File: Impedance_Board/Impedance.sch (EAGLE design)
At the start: 40 parts, among them IC1 AD8608ARZ, IC2 INA826AID, U4 MC74VHC1GT66DTT1

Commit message: Board Updates
All LEDs at same location
Separated analog and digital ground
Updated impedance components
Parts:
- C1, C13, C5, C9: device rcl:C-EUC0603 -> SparkFun-Capacitors:10UF-0603-6.3V-20%
- C12, C2, C4, C8: device rcl:C-EUC0603 -> SparkFun-Capacitors:0.1UF-0603-25V-5%
- C3: value 0.1uF -> 10nF; device SparkFun-Capacitors:0.1UF-0603-25V-(+80/-20%) -> SparkFun-Capacitors:10NF-0603-50V-10%
- R10, R9: value 47k -> 10k; device SparkFun-Resistors:47KOHM-0603-1/10W-1% -> SparkFun-Resistors:10KOHM-0603-1/10W-1%
- R11: value 1k -> 270k; device SparkFun-Resistors:1KOHM-0603-1/10W-1% -> SparkFun-Resistors:220KOHM-0603-1/10W-1%
- R5, R6: value 47k -> 100k; device SparkFun-Resistors:47KOHM-0603-1/10W-1% -> SparkFun-Resistors:100KOHM-0603-1/10W-1%
- R7: value 3.9k -> 200k; device SparkFun-Resistors:3.9KOHM-0603-1/10W-1% -> SparkFun-Resistors:200KOHM-0603-1/10W-1%
- R8: value 5.6k -> 1k; device SparkFun-Resistors:5.6KOHM-0603-1/10W-1% -> SparkFun-Resistors:1KOHM-0603-1/10W-1%
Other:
- moved on the sheet: C1, C12, C13, C2, C4, C5, C8, C9

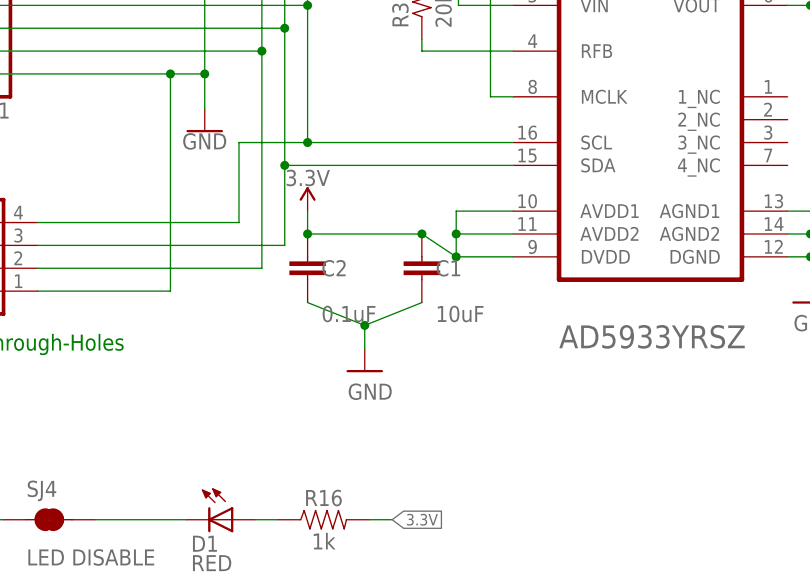
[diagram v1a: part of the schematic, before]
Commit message: Board Updates
Separated analog and digital ground
Updated routing
Updated silk labeling
Sound board with ES8388 included
Impedance and ECG board
Working on IMU board
Working on Environmental Airquality board
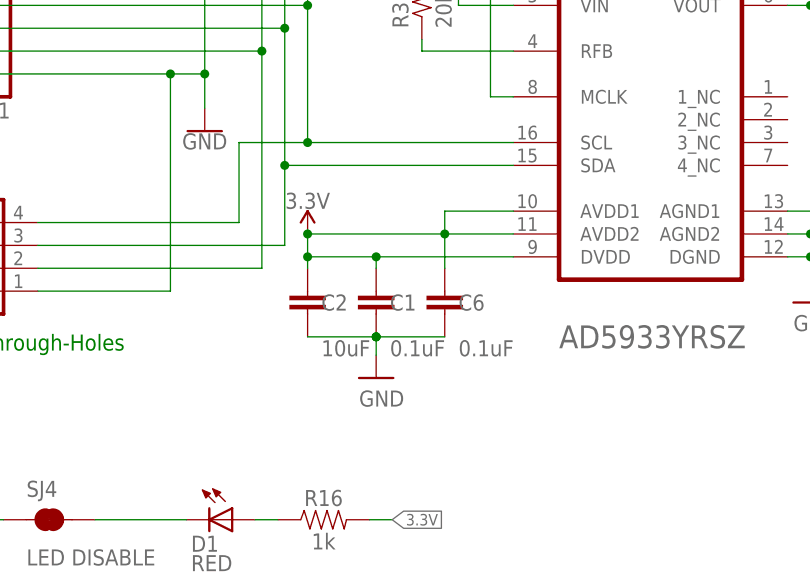
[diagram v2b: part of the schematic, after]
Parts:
- added C6: 0.1uF, SparkFun-Capacitors:0.1UF-0603-25V-(+80/-20%)
- C1: value 10uF -> 0.1uF; device SparkFun-Capacitors:10UF-0603-6.3V-20% -> SparkFun-Capacitors:0.1UF-0603-25V-(+80/-20%)
- C2: value 0.1uF -> 10uF; device SparkFun-Capacitors:0.1UF-0603-25V-5% -> SparkFun-Capacitors:10UF-0603-6.3V-20%
- SJ4: device SparkFun-Jumpers:JUMPER-SMT_2_NC_TRACE_NO-SILK -> SparkFun-Jumpers:JUMPER-SMT_2_NC_TRACE_SILK
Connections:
- net 3.3V: now also C6.1
- net GND: now also C6.2
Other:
- moved on the sheet: C1, C2
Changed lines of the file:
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@@
 <part name="R1" library="SparkFun-Resistors" library_urn="urn:adsk.eagle:library:532" deviceset="4.7KOHM" device="-0603-1/10W-1%" package3d_urn="urn:adsk.eagle:package:39650/1" value="4.7k"/>
 <part name="R2" library="SparkFun-Resistors" library_urn="urn:adsk.eagle:library:532" deviceset="4.7KOHM" device="-0603-1/10W-1%" package3d_urn="urn:adsk.eagle:package:39650/1" value="4.7k"/>
-<part name="C1" library="SparkFun-Capacitors" library_urn="urn:adsk.eagle:library:510" deviceset="10UF" device="-0603-6.3V-20%" package3d_urn="urn:adsk.eagle:package:37414/1" value="10uF"/>
-<part name="C2" library="SparkFun-Capacitors" library_urn="urn:adsk.eagle:library:510" deviceset="0.1UF" device="-0603-25V-5%" package3d_urn="urn:adsk.eagle:package:37414/1" value="0.1uF"/>
+<part name="C1" library="SparkFun-Capacitors" library_urn="urn:adsk.eagle:library:510" deviceset="0.1UF" device="-0603-25V-(+80/-20%)" package3d_urn="urn:adsk.eagle:package:37414/1" value="0.1uF"/>
+<part name="C2" library="SparkFun-Capacitors" library_urn="urn:adsk.eagle:library:510" deviceset="10UF" device="-0603-6.3V-20%" package3d_urn="urn:adsk.eagle:package:37414/1" value="10uF"/>
 <part name="R3" library="SparkFun-Resistors" library_urn="urn:adsk.eagle:library:532" deviceset="20KOHM" device="-0603-1/10W-1%" package3d_urn="urn:adsk.eagle:package:39650/1" value="20k"/>
 <part name="R4" library="SparkFun-Resistors" library_urn="urn:adsk.eagle:library:532" deviceset="20KOHM" device="-0603-1/10W-1%" package3d_urn="urn:adsk.eagle:package:39650/1" value="20k"/>
@@
 <part name="D1" library="SparkFun-LED" deviceset="LED-RED" device="0603" value="RED"/>
 <part name="GND4" library="SparkFun-Aesthetics" deviceset="GND" device=""/>
-<part name="SJ4" library="SparkFun-Jumpers" library_urn="urn:adsk.eagle:library:528" deviceset="JUMPER-SMT_2_NC_TRACE" device="_NO-SILK" package3d_urn="urn:adsk.eagle:package:39286/1" value="LED DISABLE"/>
+<part name="SJ4" library="SparkFun-Jumpers" library_urn="urn:adsk.eagle:library:528" deviceset="JUMPER-SMT_2_NC_TRACE" device="_SILK" package3d_urn="urn:adsk.eagle:package:39281/1" value="LED DISABLE"/>
 <part name="JP1" library="SparkFun-Jumpers" library_urn="urn:adsk.eagle:library:528" deviceset="JUMPER-SMT_3_1-NC_TRACE" device="_NO-SILK" package3d_urn="urn:adsk.eagle:package:39287/1"/>
 <part name="IC1" library="AD8608ARZ" deviceset="AD8608ARZ" device=""/>
@@
 <part name="FRAME1" library="SparkFun-Aesthetics" library_urn="urn:adsk.eagle:library:507" deviceset="FRAME-LETTER" device="NO_PACKAGE" package3d_urn="urn:adsk.eagle:package:37104/1"/>
 <part name="JP2" library="SparkFun-Jumpers" library_urn="urn:adsk.eagle:library:528" deviceset="JUMPER-SMT_3_1-NC_TRACE" device="_NO-SILK" package3d_urn="urn:adsk.eagle:package:39287/1"/>
+<part name="C6" library="SparkFun-Capacitors" library_urn="urn:adsk.eagle:library:510" deviceset="0.1UF" device="-0603-25V-(+80/-20%)" package3d_urn="urn:adsk.eagle:package:37414/1" value="0.1uF"/>
 </parts>
 <sheets>
@@
 <attribute name="VALUE" x="-81.534" y="36.576" size="1.778" layer="96" rot="R90"/>
 </instance>
-<instance part="C1" gate="G$1" x="-53.34" y="-21.59" smashed="yes">
-<attribute name="NAME" x="-51.816" y="-21.209" size="1.778" layer="95"/>
-<attribute name="VALUE" x="-51.816" y="-26.289" size="1.778" layer="96"/>
-</instance>
-<instance part="C2" gate="G$1" x="-66.04" y="-21.59" smashed="yes">
-<attribute name="NAME" x="-64.516" y="-21.209" size="1.778" layer="95"/>
-<attribute name="VALUE" x="-64.516" y="-26.289" size="1.778" layer="96"/>
+<instance part="C1" gate="G$1" x="-58.42" y="-25.4" smashed="yes">
+<attribute name="NAME" x="-56.896" y="-25.019" size="1.778" layer="95"/>
+<attribute name="VALUE" x="-56.896" y="-30.099" size="1.778" layer="96"/>
+</instance>
+<instance part="C2" gate="G$1" x="-66.04" y="-25.4" smashed="yes">
+<attribute name="NAME" x="-64.516" y="-25.019" size="1.778" layer="95"/>
+<attribute name="VALUE" x="-64.516" y="-30.099" size="1.778" layer="96"/>
 </instance>
 <instance part="R3" gate="G$1" x="-53.34" y="10.16" smashed="yes" rot="R90">
@@
 <attribute name="VALUE" x="12.065" y="-9.525" size="1.778" layer="96"/>
 </instance>
-<instance part="SUPPLY2" gate="1" x="-59.69" y="-31.75" smashed="yes">
-<attribute name="VALUE" x="-61.595" y="-34.925" size="1.778" layer="96"/>
-</instance>
-<instance part="SUPPLY3" gate="G$1" x="-66.04" y="-13.97" smashed="yes">
-<attribute name="VALUE" x="-66.04" y="-11.176" size="1.778" layer="96" align="bottom-center"/>
+<instance part="SUPPLY2" gate="1" x="-58.42" y="-32.512" smashed="yes">
+<attribute name="VALUE" x="-60.325" y="-35.687" size="1.778" layer="96"/>
+</instance>
+<instance part="SUPPLY3" gate="G$1" x="-66.04" y="-16.51" smashed="yes">
+<attribute name="VALUE" x="-66.04" y="-13.716" size="1.778" layer="96" align="bottom-center"/>
 </instance>
 <instance part="SUPPLY5" gate="1" x="-10.16" y="-24.13" smashed="yes">
@@
 <attribute name="NAME" x="-1.651" y="-10.16" size="1.778" layer="95" font="vector" rot="MR180"/>
 <attribute name="VALUE" x="-0.889" y="-10.16" size="1.778" layer="96" font="vector" rot="MR270" align="top-left" display="off"/>
+</instance>
+<instance part="C6" gate="G$1" x="-50.8" y="-25.4" smashed="yes">
+<attribute name="NAME" x="-49.276" y="-25.019" size="1.778" layer="95"/>
+<attribute name="VALUE" x="-49.276" y="-30.099" size="1.778" layer="96"/>
 </instance>
 </instances>
@@
 <pinref part="C2" gate="G$1" pin="2"/>
 <pinref part="C1" gate="G$1" pin="2"/>
-<wire x1="-66.04" y1="-24.13" x2="-59.69" y2="-26.67" width="0.1524" layer="91"/>
-<wire x1="-59.69" y1="-26.67" x2="-53.34" y2="-24.13" width="0.1524" layer="91"/>
-<wire x1="-59.69" y1="-26.67" x2="-59.69" y2="-29.21" width="0.1524" layer="91"/>
-<junction x="-59.69" y="-26.67"/>
+<wire x1="-66.04" y1="-27.94" x2="-58.42" y2="-27.94" width="0.1524" layer="91"/>
+<wire x1="-58.42" y1="-27.94" x2="-58.42" y2="-29.972" width="0.1524" layer="91"/>
+<junction x="-58.42" y="-27.94"/>
 <pinref part="SUPPLY2" gate="1" pin="GND"/>
+<pinref part="C6" gate="G$1" pin="2"/>
+<wire x1="-58.42" y1="-27.94" x2="-50.8" y2="-27.94" width="0.1524" layer="91"/>
+<junction x="-58.42" y="-27.94"/>
 </segment>
 <segment>
@@
 </segment>
 <segment>
+<pinref part="SUPPLY3" gate="G$1" pin="3.3V"/>
+<pinref part="C2" gate="G$1" pin="1"/>
+<wire x1="-66.04" y1="-20.32" x2="-66.04" y2="-19.05" width="0.1524" layer="91"/>
+<pinref part="AD5933" gate="G$0" pin="AVDD2"/>
+<wire x1="-66.04" y1="-19.05" x2="-66.04" y2="-16.51" width="0.1524" layer="91"/>
+<wire x1="-43.18" y1="-16.51" x2="-50.8" y2="-16.51" width="0.1524" layer="91"/>
+<pinref part="AD5933" gate="G$0" pin="AVDD1"/>
+<wire x1="-50.8" y1="-13.97" x2="-50.8" y2="-16.51" width="0.1524" layer="91"/>
+<wire x1="-43.18" y1="-13.97" x2="-50.8" y2="-13.97" width="0.1524" layer="91"/>
+<pinref part="C6" gate="G$1" pin="1"/>
+<wire x1="-50.8" y1="-20.32" x2="-50.8" y2="-16.51" width="0.1524" layer="91"/>
+<junction x="-50.8" y="-16.51"/>
+<wire x1="-66.04" y1="-16.51" x2="-50.8" y2="-16.51" width="0.1524" layer="91"/>
+<junction x="-66.04" y="-16.51"/>
+<pinref part="AD5933" gate="G$0" pin="DVDD"/>
 <pinref part="C1" gate="G$1" pin="1"/>
-<pinref part="AD5933" gate="G$0" pin="DVDD"/>
-<wire x1="-53.34" y1="-16.51" x2="-49.53" y2="-19.05" width="0.1524" layer="91"/>
-<pinref part="AD5933" gate="G$0" pin="AVDD2"/>
-<wire x1="-49.53" y1="-19.05" x2="-43.18" y2="-19.05" width="0.1524" layer="91"/>
-<wire x1="-43.18" y1="-16.51" x2="-49.53" y2="-16.51" width="0.1524" layer="91"/>
-<wire x1="-49.53" y1="-16.51" x2="-49.53" y2="-19.05" width="0.1524" layer="91"/>
-<junction x="-49.53" y="-19.05"/>
-<pinref part="AD5933" gate="G$0" pin="AVDD1"/>
-<wire x1="-43.18" y1="-13.97" x2="-49.53" y2="-13.97" width="0.1524" layer="91"/>
-<wire x1="-49.53" y1="-13.97" x2="-49.53" y2="-16.51" width="0.1524" layer="91"/>
-<junction x="-49.53" y="-16.51"/>
-<pinref part="C2" gate="G$1" pin="1"/>
-<wire x1="-66.04" y1="-16.51" x2="-53.34" y2="-16.51" width="0.1524" layer="91"/>
-<junction x="-53.34" y="-16.51"/>
-<wire x1="-66.04" y1="-16.51" x2="-66.04" y2="-13.97" width="0.1524" layer="91"/>
-<junction x="-66.04" y="-16.51"/>
-<pinref part="SUPPLY3" gate="G$1" pin="3.3V"/>
-</segment>
-<segment>
+<wire x1="-43.18" y1="-19.05" x2="-58.42" y2="-19.05" width="0.1524" layer="91"/>
+<wire x1="-58.42" y1="-19.05" x2="-58.42" y2="-20.32" width="0.1524" layer="91"/>
+<wire x1="-58.42" y1="-19.05" x2="-66.04" y2="-19.05" width="0.1524" layer="91"/>
+<junction x="-58.42" y="-19.05"/>
+<junction x="-66.04" y="-19.05"/>
+</segment>
+<segment>

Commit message: Production Updates
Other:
- note added: "AMP_FB"
- note added: "Amp_Buffer"
- note added: "Amp_REFGEN"
- note added: "Amp_VCC"
- moved on the sheet: C12, C13, C4, C5, C8, C9
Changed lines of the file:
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@@
 <drawing>
 <settings>
-<setting alwaysvectorfont="no"/>
+<setting alwaysvectorfont="yes"/>
 <setting verticaltext="up"/>
 </settings>
@@
 <text x="24.638" y="32.258" size="1.778" layer="91">Switch
 Direct vs Transimpedance</text>
+<text x="55.88" y="40.64" size="1.778" layer="91">Amp_VCC</text>
+<text x="55.88" y="45.72" size="1.778" layer="91">Amp_REFGEN</text>
+<text x="38.1" y="45.72" size="1.778" layer="91">Amp_Buffer</text>
+<text x="38.1" y="40.64" size="1.778" layer="91">AMP_FB</text>
 </plain>
 <instances>
@@
 <attribute name="VALUE" x="20.574" y="-11.176" size="1.778" layer="96" rot="MR0" align="bottom-center"/>
 </instance>
-<instance part="C4" gate="G$1" x="20.574" y="-19.05" smashed="yes" rot="MR0">
-<attribute name="NAME" x="19.05" y="-18.669" size="1.778" layer="95" rot="MR0"/>
-<attribute name="VALUE" x="19.05" y="-23.749" size="1.778" layer="96" rot="MR0"/>
-</instance>
-<instance part="C5" gate="G$1" x="9.144" y="-19.05" smashed="yes" rot="MR0">
-<attribute name="NAME" x="7.62" y="-18.669" size="1.778" layer="95" rot="MR0"/>
-<attribute name="VALUE" x="7.62" y="-23.749" size="1.778" layer="96" rot="MR0"/>
+<instance part="C4" gate="G$1" x="20.574" y="-21.59" smashed="yes" rot="MR0">
+<attribute name="NAME" x="19.05" y="-21.209" size="1.778" layer="95" rot="MR0"/>
+<attribute name="VALUE" x="19.05" y="-26.289" size="1.778" layer="96" rot="MR0"/>
+</instance>
+<instance part="C5" gate="G$1" x="9.144" y="-21.59" smashed="yes" rot="MR0">
+<attribute name="NAME" x="7.62" y="-21.209" size="1.778" layer="95" rot="MR0"/>
+<attribute name="VALUE" x="7.62" y="-26.289" size="1.778" layer="96" rot="MR0"/>
 </instance>
 <instance part="SUPPLY8" gate="1" x="14.224" y="-29.21" smashed="yes" rot="MR0">
@@
 <attribute name="VALUE" x="88.265" y="-44.831" size="1.778" layer="96"/>
 </instance>
-<instance part="C8" gate="G$1" x="16.51" y="46.99" smashed="yes" rot="MR0">
-<attribute name="NAME" x="14.986" y="47.371" size="1.778" layer="95" rot="MR0"/>
-<attribute name="VALUE" x="14.986" y="42.291" size="1.778" layer="96" rot="MR0"/>
-</instance>
-<instance part="C9" gate="G$1" x="8.89" y="46.99" smashed="yes" rot="MR0">
-<attribute name="NAME" x="7.366" y="47.371" size="1.778" layer="95" rot="MR0"/>
-<attribute name="VALUE" x="7.366" y="42.291" size="1.778" layer="96" rot="MR0"/>
+<instance part="C8" gate="G$1" x="16.51" y="44.45" smashed="yes" rot="MR0">
+<attribute name="NAME" x="14.986" y="44.831" size="1.778" layer="95" rot="MR0"/>
+<attribute name="VALUE" x="14.986" y="39.751" size="1.778" layer="96" rot="MR0"/>
+</instance>
+<instance part="C9" gate="G$1" x="8.89" y="44.45" smashed="yes" rot="MR0">
+<attribute name="NAME" x="7.366" y="44.831" size="1.778" layer="95" rot="MR0"/>
+<attribute name="VALUE" x="7.366" y="39.751" size="1.778" layer="96" rot="MR0"/>
 </instance>
 <instance part="SUPPLY14" gate="G$1" x="16.51" y="50.8" smashed="yes" rot="MR0">
@@
 <attribute name="VALUE" x="-55.88" y="20.32" size="1.778" layer="96" font="vector" rot="MR0" display="off"/>
 </instance>
-<instance part="C12" gate="G$1" x="-55.88" y="41.91" smashed="yes" rot="MR0">
-<attribute name="NAME" x="-57.404" y="42.291" size="1.778" layer="95" rot="MR0"/>
-<attribute name="VALUE" x="-57.404" y="37.211" size="1.778" layer="96" rot="MR0"/>
-</instance>
-<instance part="C13" gate="G$1" x="-63.5" y="41.91" smashed="yes" rot="MR0">
-<attribute name="NAME" x="-65.024" y="42.291" size="1.778" layer="95" rot="MR0"/>
-<attribute name="VALUE" x="-65.024" y="37.211" size="1.778" layer="96" rot="MR0"/>
+<instance part="C12" gate="G$1" x="-55.88" y="39.37" smashed="yes" rot="MR0">
+<attribute name="NAME" x="-57.404" y="39.751" size="1.778" layer="95" rot="MR0"/>
+<attribute name="VALUE" x="-57.404" y="34.671" size="1.778" layer="96" rot="MR0"/>
+</instance>
+<instance part="C13" gate="G$1" x="-63.5" y="39.37" smashed="yes" rot="MR0">
+<attribute name="NAME" x="-65.024" y="39.751" size="1.778" layer="95" rot="MR0"/>
+<attribute name="VALUE" x="-65.024" y="34.671" size="1.778" layer="96" rot="MR0"/>
 </instance>
 <instance part="SUPPLY26" gate="1" x="-59.69" y="31.75" smashed="yes" rot="MR0">
@@
 <pinref part="C4" gate="G$1" pin="2"/>
 <pinref part="C5" gate="G$1" pin="2"/>
-<wire x1="20.574" y1="-21.59" x2="14.224" y2="-24.13" width="0.1524" layer="91"/>
-<wire x1="14.224" y1="-24.13" x2="9.144" y2="-21.59" width="0.1524" layer="91"/>
+<wire x1="20.574" y1="-24.13" x2="14.224" y2="-24.13" width="0.1524" layer="91"/>
+<wire x1="14.224" y1="-24.13" x2="9.144" y2="-24.13" width="0.1524" layer="91"/>
 <wire x1="14.224" y1="-24.13" x2="14.224" y2="-26.67" width="0.1524" layer="91"/>
 <junction x="14.224" y="-24.13"/>
@@
 <pinref part="SUPPLY15" gate="1" pin="GND"/>
 <pinref part="C8" gate="G$1" pin="2"/>
-<wire x1="16.51" y1="44.45" x2="12.7" y2="41.91" width="0.1524" layer="91"/>
+<wire x1="16.51" y1="41.91" x2="12.7" y2="41.91" width="0.1524" layer="91"/>
 <wire x1="12.7" y1="41.91" x2="12.7" y2="39.37" width="0.1524" layer="91"/>
 <junction x="12.7" y="41.91"/>
-<wire x1="12.7" y1="41.91" x2="8.89" y2="44.45" width="0.1524" layer="91"/>
+<wire x1="12.7" y1="41.91" x2="8.89" y2="41.91" width="0.1524" layer="91"/>
 </segment>
 <segment>
@@
 <pinref part="C12" gate="G$1" pin="2"/>
 <pinref part="C13" gate="G$1" pin="2"/>
-<wire x1="-55.88" y1="39.37" x2="-59.69" y2="36.83" width="0.1524" layer="91"/>
-<wire x1="-59.69" y1="36.83" x2="-63.5" y2="39.37" width="0.1524" layer="91"/>
+<wire x1="-55.88" y1="36.83" x2="-59.69" y2="36.83" width="0.1524" layer="91"/>
+<wire x1="-59.69" y1="36.83" x2="-63.5" y2="36.83" width="0.1524" layer="91"/>
 <wire x1="-59.69" y1="36.83" x2="-59.69" y2="34.29" width="0.1524" layer="91"/>
 <junction x="-59.69" y="36.83"/>
@@
 <pinref part="SUPPLY7" gate="G$1" pin="3.3V"/>
 <pinref part="C4" gate="G$1" pin="1"/>
-<wire x1="20.574" y1="-13.97" x2="9.144" y2="-13.97" width="0.1524" layer="91"/>
-<junction x="20.574" y="-13.97"/>
+<wire x1="20.574" y1="-16.51" x2="9.144" y2="-16.51" width="0.1524" layer="91"/>
+<junction x="20.574" y="-16.51"/>
 <pinref part="C5" gate="G$1" pin="1"/>
 <pinref part="IC2" gate="G$1" pin="+VS"/>
 <wire x1="63.5" y1="-20.32" x2="64.77" y2="-20.32" width="0.1524" layer="91"/>
 <wire x1="64.77" y1="-20.32" x2="64.77" y2="-16.51" width="0.1524" layer="91"/>
-<wire x1="64.77" y1="-16.51" x2="20.574" y2="-13.97" width="0.1524" layer="91"/>
-<wire x1="20.32" y1="-16.51" x2="20.574" y2="-13.97" width="0.1524" layer="91"/>
+<wire x1="64.77" y1="-16.51" x2="20.574" y2="-16.51" width="0.1524" layer="91"/>
+<wire x1="20.32" y1="-16.51" x2="20.574" y2="-16.51" width="0.1524" layer="91"/>
+<wire x1="20.574" y1="-16.51" x2="20.574" y2="-13.97" width="0.1524" layer="91"/>
 </segment>
 <segment>
@@
 </segment>
 <segment>
-<wire x1="16.51" y1="52.07" x2="16.51" y2="50.8" width="0.1524" layer="91"/>
+<wire x1="16.51" y1="49.53" x2="16.51" y2="50.8" width="0.1524" layer="91"/>
 <pinref part="C8" gate="G$1" pin="1"/>
-<wire x1="16.51" y1="52.07" x2="8.89" y2="52.07" width="0.1524" layer="91"/>
-<junction x="16.51" y="52.07"/>
+<wire x1="16.51" y1="49.53" x2="8.89" y2="49.53" width="0.1524" layer="91"/>
+<junction x="16.51" y="49.53"/>
 <pinref part="C9" gate="G$1" pin="1"/>
 <pinref part="SUPPLY14" gate="G$1" pin="3.3V"/>
@@
 <wire x1="20.574" y1="49.53" x2="20.574" y2="6.35" width="0.1524" layer="91"/>
 <wire x1="20.574" y1="6.35" x2="35.814" y2="6.35" width="0.1524" layer="91"/>
-<wire x1="16.51" y1="52.07" x2="20.574" y2="49.53" width="0.1524" layer="91"/>
+<wire x1="16.51" y1="49.53" x2="20.574" y2="49.53" width="0.1524" layer="91"/>
 </segment>
 <segment>
@@
 <pinref part="C13" gate="G$1" pin="1"/>
 <pinref part="C12" gate="G$1" pin="1"/>
-<wire x1="-55.88" y1="46.99" x2="-63.5" y2="46.99" width="0.1524" layer="91"/>
-<junction x="-55.88" y="46.99"/>
+<wire x1="-55.88" y1="44.45" x2="-63.5" y2="44.45" width="0.1524" layer="91"/>
+<junction x="-55.88" y="44.45"/>
 <pinref part="U4" gate="A" pin="5"/>
 <wire x1="-10.16" y1="40.64" x2="-7.62" y2="40.64" width="0.1524" layer="91"/>
 <wire x1="-7.62" y1="40.64" x2="-7.62" y2="49.53" width="0.1524" layer="91"/>
 <wire x1="-7.62" y1="49.53" x2="-55.88" y2="49.53" width="0.1524" layer="91"/>
-<wire x1="-55.88" y1="49.53" x2="-55.88" y2="46.99" width="0.1524" layer="91"/>
+<wire x1="-55.88" y1="49.53" x2="-55.88" y2="44.45" width="0.1524" layer="91"/>
 <pinref part="SUPPLY23" gate="G$1" pin="3.3V"/>
-<wire x1="-63.5" y1="46.99" x2="-63.5" y2="45.212" width="0.1524" layer="91"/>
-<junction x="-63.5" y="46.99"/>
+<wire x1="-63.5" y1="44.45" x2="-63.5" y2="45.212" width="0.1524" layer="91"/>
+<junction x="-63.5" y="44.45"/>
 </segment>
 </net>
@@
 </segment>
 </net>
+<net name="N$7" class="0">
+<segment>
+<wire x1="35.56" y1="48.26" x2="35.56" y2="43.18" width="0.1524" layer="91"/>
+<wire x1="35.56" y1="43.18" x2="35.56" y2="38.1" width="0.1524" layer="91"/>
+<wire x1="35.56" y1="38.1" x2="53.34" y2="38.1" width="0.1524" layer="91"/>
+<wire x1="53.34" y1="38.1" x2="71.12" y2="38.1" width="0.1524" layer="91"/>
+<wire x1="71.12" y1="38.1" x2="71.12" y2="43.18" width="0.1524" layer="91"/>
+<wire x1="71.12" y1="43.18" x2="71.12" y2="48.26" width="0.1524" layer="91"/>
+<wire x1="71.12" y1="48.26" x2="53.34" y2="48.26" width="0.1524" layer="91"/>
+<wire x1="53.34" y1="48.26" x2="35.56" y2="48.26" width="0.1524" layer="91"/>
+<wire x1="53.34" y1="48.26" x2="53.34" y2="38.1" width="0.1524" layer="91"/>
+<wire x1="35.56" y1="43.18" x2="71.12" y2="43.18" width="0.1524" layer="91"/>
+</segment>
+</net>
